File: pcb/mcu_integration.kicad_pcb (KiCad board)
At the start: 4 copper layers, 90.2 x 95.9 mm, 104 parts, among them IC1 TL7660IDGKR, IC10 AD844_OPAMP_MEL, IC2 TL081IDT, IC3 FOD814_OPTO_NOSHD, IC5 FOD814_OPTO_MEL, IC6 AD844_OPAMP_AL, IC7 FOD814_OPTO_AL, IC8 AD844_OPAMP_NOSHD, IC9 TL081IDT, J4 Conn_01x02, J5 DM3BT-DSF-PEJS, M1 MountingHole_Pad, M2 MountingHole_Pad, M3 MountingHole_Pad, M4 MountingHole_Pad, U1 STM32F103RBTx, U2 REF192_NOSHD, U3 REF192_AL, U4 REF192_MEL, U5 TPS2069CDBVR_MOSFET, U6 LM35DM

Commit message: Restructured PCB
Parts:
- removed C19, C20, C34, C38, C41: 0.1u, capstone:CAPC220145_88N_KEM-0.1u
- removed C21, C37: 1u, capstone:C0805-1u
- removed C23, C24: 10u, capstone:T495D
- removed C27: 100n, Capacitor_SMD:C_0402_1005Metric
- removed C33: 1u, Capacitor_SMD:C_0402_1005Metric
- removed C35, C36, C39, C40: 0.22u, capstone:C0805-0.22u
- removed C42: 150u, capstone:CAPC3225X280N_150U
- removed H1, H2: ESQ-126-39-L-D, capstone:ESQ-126-Y-X-D
- removed IC10: AD844_OPAMP_MEL, capstone:SOIC127P1032X265-16N-AD844
- removed IC3: FOD814_OPTO_NOSHD, capstone:SOP254P1016X385-4N-FOD
- removed IC5: FOD814_OPTO_MEL, capstone:SOP254P1016X385-4N-FOD
- removed IC8: AD844_OPAMP_NOSHD, capstone:SOIC127P1032X265-16N-AD844
- removed J4: Conn_01x02, Connector_PinHeader_2.54mm:PinHeader_1x02_P2.54mm_Vertical
- removed J5: DM3BT-DSF-PEJS, capstone:DM3BT_DSF_PEJS
- removed J_AD1, J_AD3: Conn_01x04, Connector_PinHeader_2.54mm:PinHeader_1x04_P2.54mm_Vertical
- removed M1, M2, M3, M4: MountingHole_Pad, MountingHole:MountingHole_3.2mm_M3_Pad_Via
- removed R15, R19: 820, Resistor_SMD:R_0402_1005Metric
- removed R16, R20: 47, Resistor_SMD:R_0402_1005Metric
- removed R17, R18, R29, R30: 100, Resistor_SMD:R_0402_1005Metric
- removed R28, R34: 100k, Resistor_SMD:R_0402_1005Metric
- removed R31, R35: 1k, Resistor_SMD:R_0402_1005Metric
- removed R33: 200, Resistor_SMD:R_0402_1005Metric
- removed U2: REF192_NOSHD, capstone:R_8_ADI-REF
- removed U4: REF192_MEL, capstone:R_8_ADI-REF
- removed U5: TPS2069CDBVR_MOSFET, capstone:DBV5_TEX_MF
- added PWR1: Conn_01x03, Connector_PinHeader_2.54mm:PinHeader_1x03_P2.54mm_Vertical, F.Cu at (142.6, 73.7)
- moved C22 44.4 mm to (193.3, 87.1)
- moved C29 44.4 mm to (201.1, 88.6)
- moved C32 44.4 mm to (193.3, 101.0)
- moved IC6 44.4 mm to (203.5, 96.2)
- moved IC7 44.4 mm to (185.4, 97.2)
- moved R25 44.4 mm to (209.6, 96.2)
- moved U3 44.4 mm to (193.3, 96.2)
- moved C28 44.4 mm to (193.3, 91.4)
- moved C30 44.4 mm to (206.3, 103.9)
- moved C31 44.4 mm to (193.2, 103.8)
- moved J_AD2 44.4 mm to (201.7, 113.2)
- moved R23 44.4 mm to (183.6, 103.8)
- moved R22 44.4 mm to (205.5, 89.6)
- moved R26 44.4 mm to (183.7, 90.1)
- moved R27 44.4 mm to (187.2, 90.1)
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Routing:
- net ADC1_IN0_SINE: track 215.7 -> 70.1 mm, vias 12 -> 5
- net -5V Output: track 172.1 -> 27.0 mm, vias 11 -> 3
- net 3.3V Output: track 109.1 -> 6.49 mm, vias 6 -> 0
- net GND: track 182.1 -> 85.8 mm, vias 41 -> 16
- net ADC1_IN1_OPAMP_NOSHD: track 90.3 -> 0.00 mm, vias 3 -> 0
- net ADC1_IN4_VREF_NOSHD: track 87.9 -> 0.00 mm
- net ADC1_IN12_OPTO_F_MEL: track 74.2 -> 0.00 mm, vias 2 -> 0
- net ADC1_IN5_VREF_MEL: track 68.0 -> 0.00 mm
- net ADC1_IN13_OPTO_E_MEL: track 63.2 -> 0.00 mm, vias 4 -> 0
- net +5V_EXT: track 56.5 -> 0.00 mm
- net ADC1_IN11_OPTO_E_NOSHD: track 52.8 -> 0.00 mm
- net ADC1_IN2_OPAMP_MEL: track 52.1 -> 0.00 mm, vias 4 -> 0
- net SIG_SQUARE: track 57.8 -> 6.64 mm, vias 3 -> 0
- net ADC1_IN3_OPAMP_AL: track 67.8 -> 25.6 mm, vias 2 -> 1
- net +5V: track 70.7 -> 29.3 mm, vias 17 -> 8
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- removed copper zone on In2.Cu, net +5V
- removed copper zone on In1.Cu, net GND
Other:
- board size 90.2 x 95.9 mm -> 50 x 50 mm

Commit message: Arranged components to fit board
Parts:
- C22, C28, C29, C30, C31, C32, IC6, IC7, R22, R23, R24, R25, R26, R27, U3: moved to B.Cu
- moved J_AD2 80.9 mm to (124.8, 88.1), turned to 0 degrees
- moved C30 75.1 mm to (134.1, 83.4), turned to 90 degrees
- moved R25 69.6 mm to (141.8, 80.2), turned to 0 degrees
- moved IC6 62.5 mm to (141.8, 86.3), turned to 180 degrees
- moved C31 59.4 mm to (134.2, 96.6), turned to 90 degrees
- moved R22 57.3 mm to (148.4, 84.3), turned to -90 degrees
- moved C32 56.5 mm to (137.0, 96.5), turned to 90 degrees
- moved C14 54.2 mm to (121.5, 105.8)
- moved C15 54.2 mm to (125.0, 105.8)
- moved C16 54.2 mm to (128.5, 105.8)
- moved C17 54.2 mm to (132.0, 105.8)
- moved C44 54.2 mm to (143.0, 105.8)
- moved J_SIG1 54.2 mm to (136.5, 107.5)
- moved C18 54.2 mm to (144.5, 116.4)
- moved C43 54.2 mm to (136.5, 112.0)
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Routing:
- net GND: track 85.8 -> 0.00 mm, vias 16 -> 0
- net ADC1_IN0_SINE: track 70.1 -> 0.00 mm, vias 5 -> 0
- net ADC1_IN15_OPTO_E_AL: track 35.3 -> 0.00 mm
- net ADC1_IN6_VREF_AL: track 32.8 -> 0.00 mm, vias 2 -> 0
- net +5V: track 29.3 -> 0.00 mm, vias 8 -> 0
- net -5V Output: track 27.0 -> 0.00 mm, vias 3 -> 0
- net ADC1_IN3_OPAMP_AL: track 25.6 -> 0.00 mm, vias 1 -> 0
- net ADC1_IN14_OPTO_F_AL: track 19.0 -> 0.00 mm, vias 2 -> 0
- net INVERT_SINE: track 18.7 -> 0.00 mm
- net RC_OUTPUT: track 13.8 -> 0.00 mm
- net Net-(IC9-INVERTING_INPUT): track 13.3 -> 0.00 mm
- net Net-(IC6--IN): track 9.63 -> 0.00 mm
- net Net-(IC2-INVERTING_INPUT): track 7.09 -> 0.00 mm
- net SIG_SQUARE: track 6.64 -> 0.00 mm
- net Net-(J_SIG1-Pin_1): track 6.61 -> 0.00 mm
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
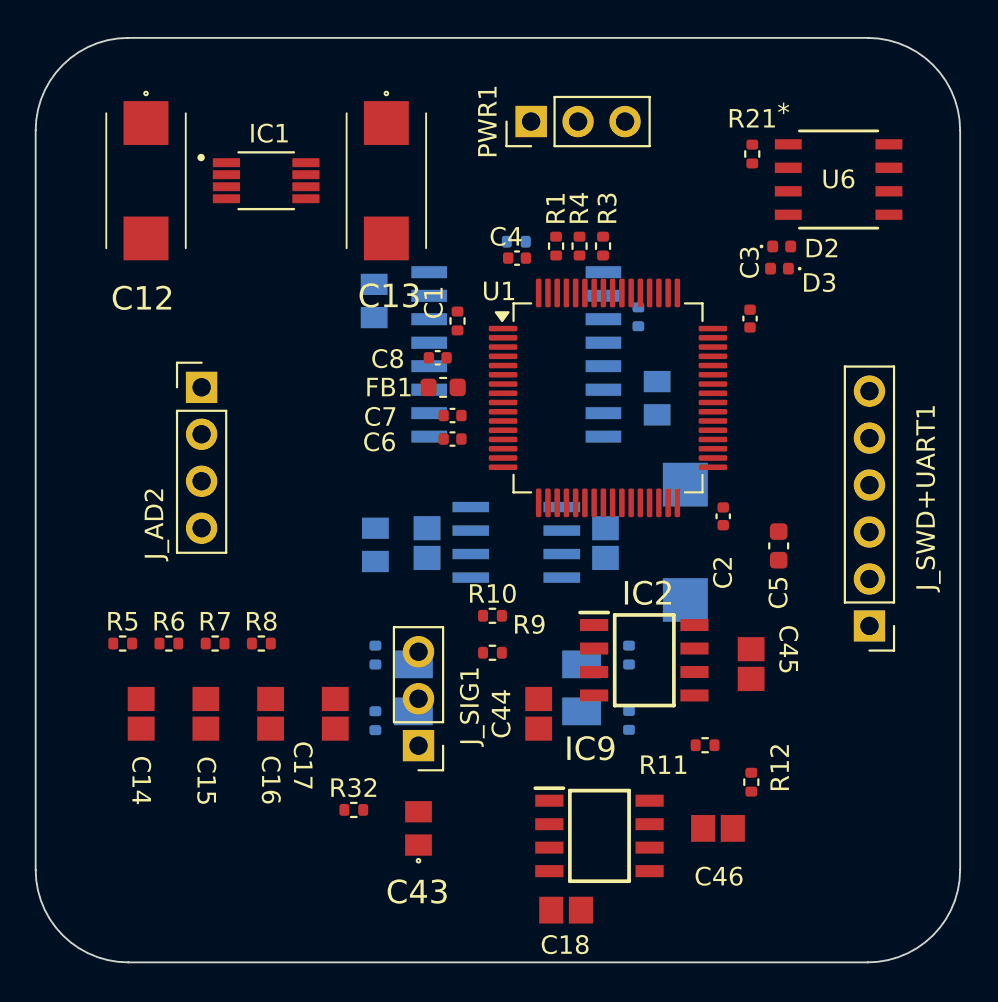
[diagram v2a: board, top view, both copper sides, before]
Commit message: Added two pin connector, routed all connections
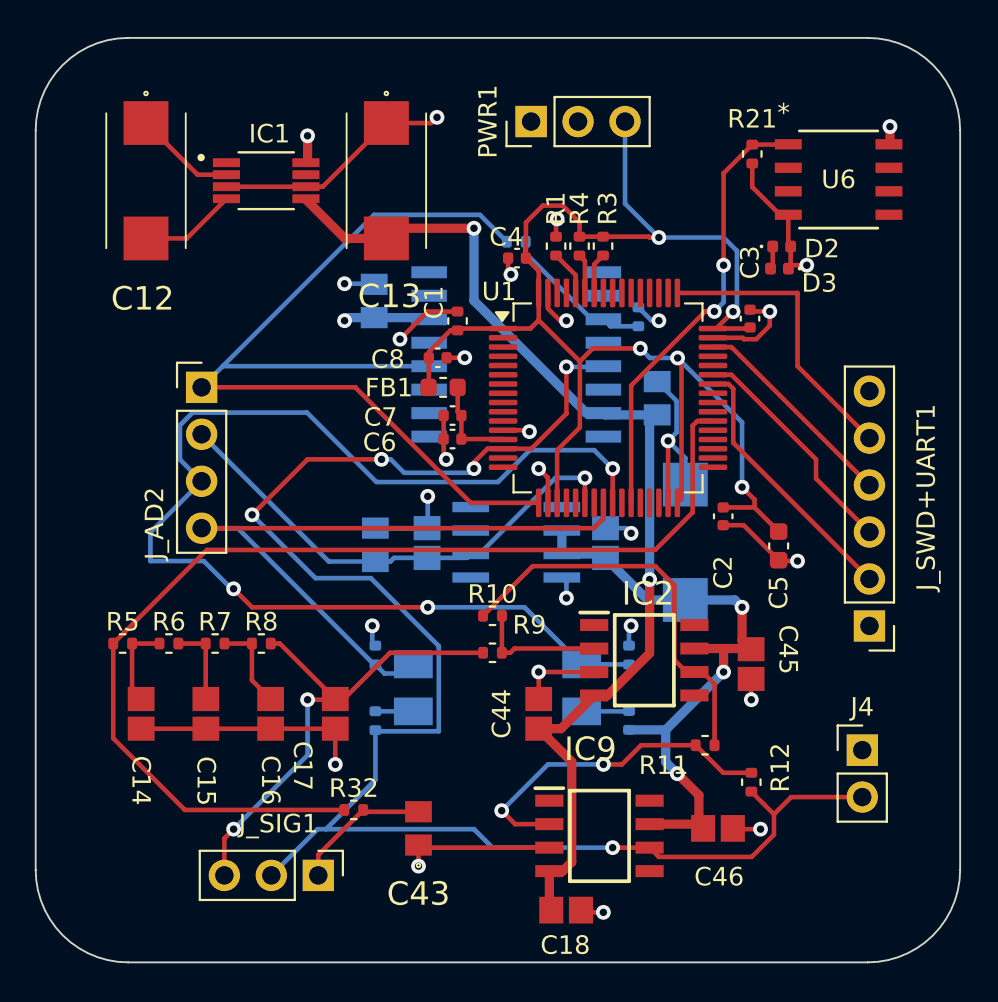
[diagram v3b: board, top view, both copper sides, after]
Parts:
- added J4: Conn_01x02, Connector_PinHeader_2.54mm:PinHeader_1x02_P2.54mm_Vertical, F.Cu at (160.5, 107.7)
- moved J_SIG1 8.86 mm to (131.1, 114.5), turned to -90 degrees
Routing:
- net GND: track 0.00 -> 97.2 mm, vias 0 -> 26
- net ADC1_IN0_SINE: track 0.00 -> 89.5 mm, vias 0 -> 5
- net 3.3V Output: track 0.00 -> 79.8 mm, vias 0 -> 5
- net ADC1_IN15_OPTO_E_AL: track 0.00 -> 65.4 mm, vias 0 -> 3
- net SIG_SQUARE: track 0.00 -> 59.4 mm
- net -5V Output: track 0.00 -> 59.0 mm, vias 0 -> 2
- net ADC1_IN3_OPAMP_AL: track 0.00 -> 53.0 mm
- net +5V: track 0.00 -> 41.7 mm, vias 0 -> 6
- net ADC1_IN14_OPTO_F_AL: track 0.00 -> 37.8 mm
- net ADC1_IN6_VREF_AL: track 0.00 -> 26.8 mm, vias 0 -> 1
- net RC_OUTPUT: track 0.00 -> 26.6 mm, vias 0 -> 2
- net ADC1_IN9_VREG_AL: track 0.00 -> 24.3 mm, vias 0 -> 2
- net INVERT_SINE: track 0.00 -> 22.0 mm
- net Net-(IC9-INVERTING_INPUT): track 0.00 -> 18.5 mm, vias 0 -> 2
- net /SWCLK: track 0.00 -> 16.0 mm
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- added copper zone on In2.Cu, net +5V
- added copper zone on In1.Cu, net GND

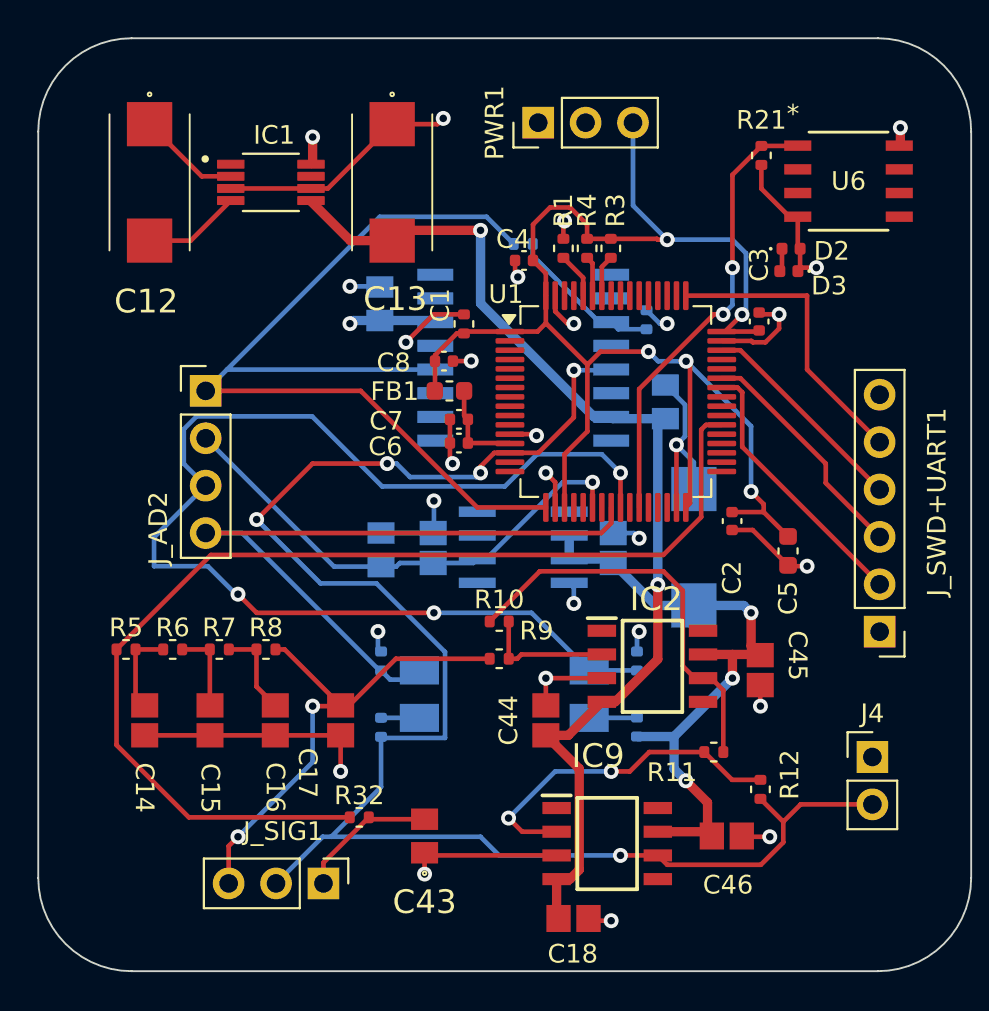
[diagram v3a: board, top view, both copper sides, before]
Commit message: Added I2C Connector
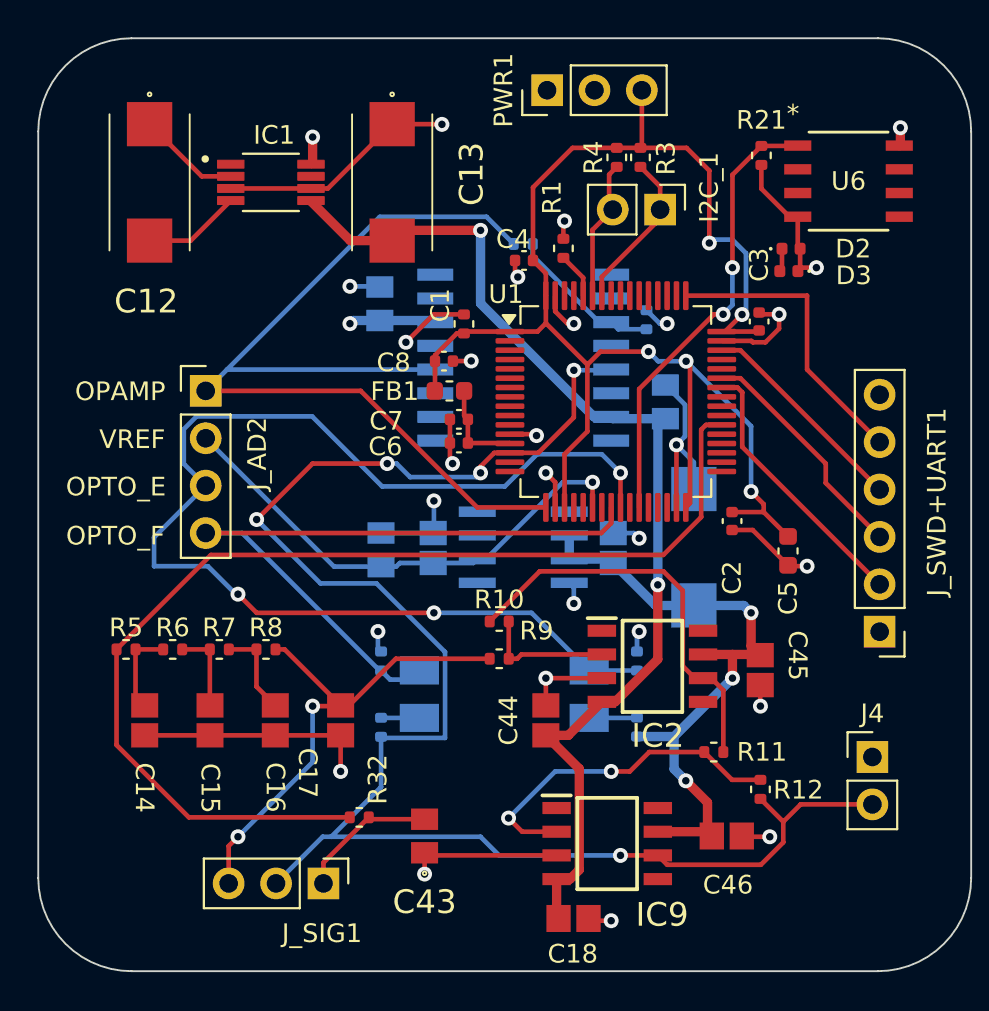
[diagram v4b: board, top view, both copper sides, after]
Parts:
- added I2C_1: Conn_01x02, Connector_PinHeader_2.54mm:PinHeader_1x02_P2.54mm_Vertical, F.Cu at (149.1, 78.4)
- moved R3 5.13 mm to (148.1, 75.6)
- moved R4 5.13 mm to (146.8, 75.6)
- moved PWR1 1.80 mm to (143.1, 72.0)
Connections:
- PWR1 pad 2: +5V_EXT -> +5V
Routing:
- net OBC_I2C_SCL: track 2.22 -> 8.63 mm
- net OBC_I2C_SDA: track 2.15 -> 7.60 mm
- net 3.3V Output: track 79.8 -> 81.6 mm
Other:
- board text added: "OPAMP"
- board text added: "OPTO_E"
- board text added: "OPTO_F"
- board text added: "VREF"

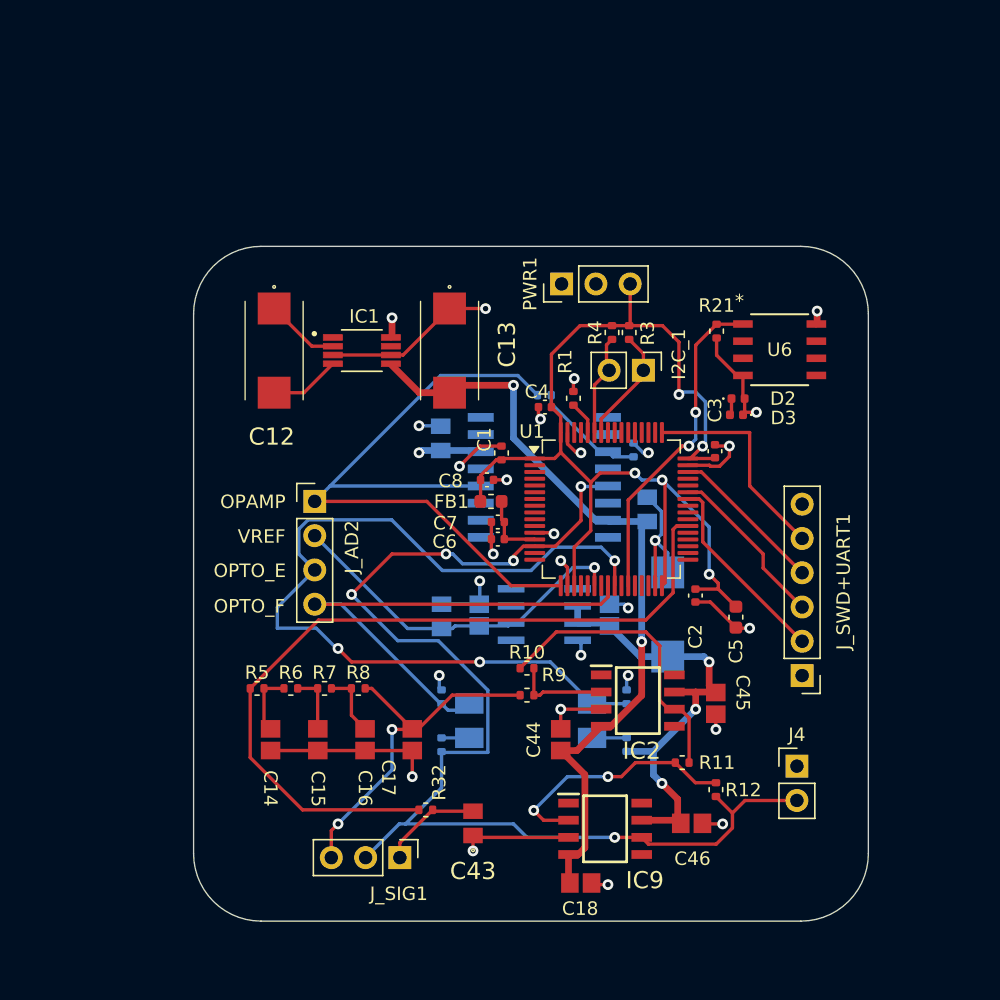
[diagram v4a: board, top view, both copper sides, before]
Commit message: Increased board size from 5x5 to 7x7
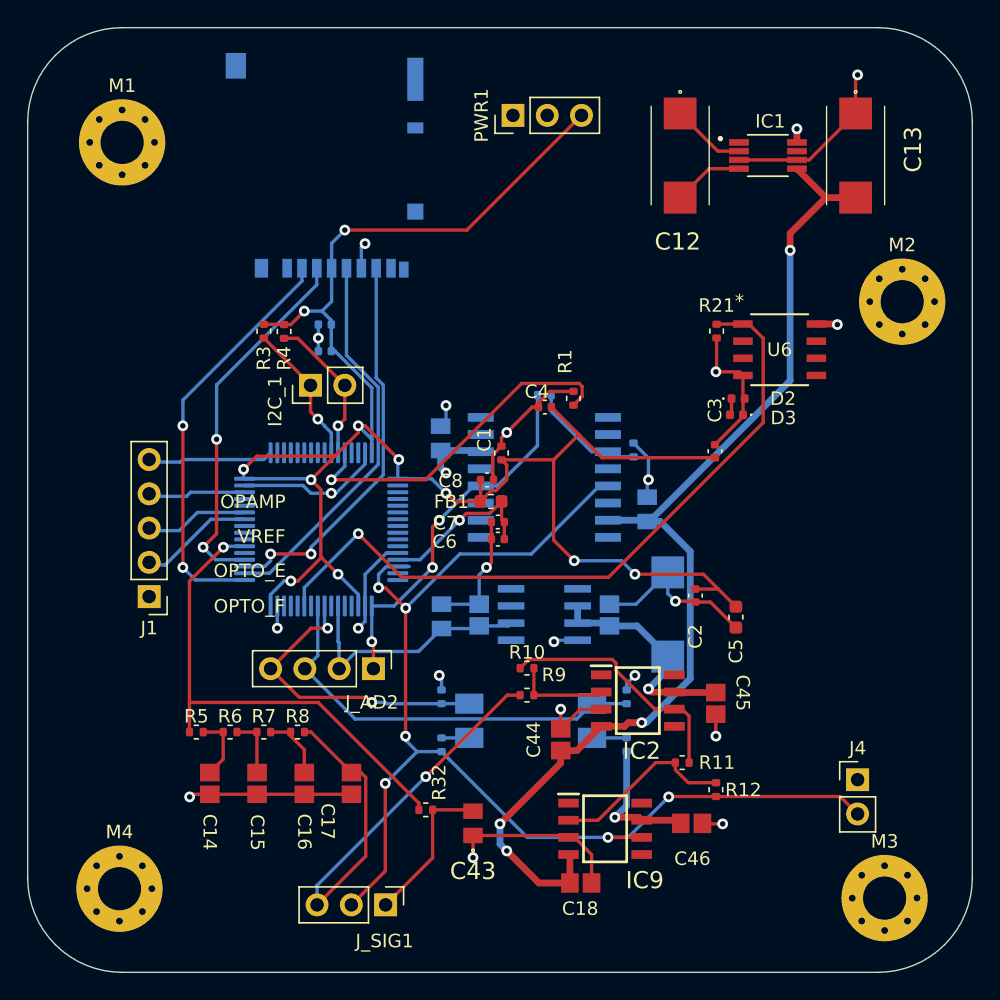
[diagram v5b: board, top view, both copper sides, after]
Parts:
- removed J_SWD+UART1: Conn_01x06, Connector_PinHeader_2.54mm:PinHeader_1x06_P2.54mm_Vertical
- added C27: 100n, Capacitor_SMD:C_0402_1005Metric, B.Cu at (125.5, 75.0)
- added C33: 1u, Capacitor_SMD:C_0402_1005Metric, B.Cu at (125.5, 77.0)
- added J1: Conn_01x05, Connector_PinHeader_2.54mm:PinHeader_1x05_P2.54mm_Vertical, F.Cu at (112.5, 95.2)
- added J5: DM3BT-DSF-PEJS, capstone:DM3BT_DSF_PEJS, B.Cu at (125.5, 63.0)
- added M1: MountingHole_Pad, MountingHole:MountingHole_3.2mm_M3_Pad_Via, F.Cu at (110.5, 61.5)
- added M2: MountingHole_Pad, MountingHole:MountingHole_3.2mm_M3_Pad_Via, F.Cu at (168.3, 73.3)
- added M3: MountingHole_Pad, MountingHole:MountingHole_3.2mm_M3_Pad_Via, F.Cu at (167.0, 117.5)
- added M4: MountingHole_Pad, MountingHole:MountingHole_3.2mm_M3_Pad_Via, F.Cu at (110.3, 116.8)
- U1: moved to B.Cu
- moved C13 33.4 mm to (164.8, 62.5)
- moved IC1 33.4 mm to (158.3, 62.5)
- moved C12 33.4 mm to (151.8, 62.5)
- moved R3 27.1 mm to (121.0, 75.5)
- moved I2C_1 24.7 mm to (124.5, 79.5), turned to 90 degrees
- moved R4 24.3 mm to (122.5, 75.5)
- moved U1 21.6 mm to (125.2, 90.2), turned to 180 degrees
- moved J_AD2 13.1 mm to (129.1, 100.5), turned to -90 degrees
- moved PWR1 13.0 mm to (139.5, 59.5)
- moved R5 5.54 mm to (116.0, 105.2)
- moved R6 5.54 mm to (118.5, 105.2)
- moved R7 5.54 mm to (121.0, 105.2)
- moved R8 5.54 mm to (123.5, 105.2)
- moved C14 5.54 mm to (117.0, 109.0)
- moved C15 5.54 mm to (120.5, 109.0)
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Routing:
- net 3.3V Output: track 81.6 -> 142.5 mm, vias 5 -> 11
- net ADC1_IN15_OPTO_E_AL: track 65.4 -> 30.9 mm, vias 3 -> 0
- net /SPI2_CS_NSS: track 0.00 -> 30.8 mm, vias 0 -> 2
- net /SPI2_MISO: track 0.00 -> 29.2 mm, vias 0 -> 2
- net ADC1_IN9_VREG_AL: track 24.3 -> 53.2 mm, vias 2 -> 1
- net /SPI2_SCK: track 0.00 -> 28.8 mm
- net /SPI2_MOSI: track 0.00 -> 27.6 mm, vias 0 -> 2
- net GND: track 97.0 -> 123.9 mm, vias 26 -> 20
- net ADC1_IN3_OPAMP_AL: track 53.0 -> 27.4 mm, vias 0 -> 3
- net /BOOT0: track 2.46 -> 25.7 mm, vias 0 -> 1
- net SIG_SQUARE: track 59.4 -> 36.9 mm, vias 0 -> 1
- net -5V Output: track 59.0 -> 80.4 mm, vias 2 -> 4
- net ADC1_IN14_OPTO_F_AL: track 37.8 -> 23.0 mm, vias 0 -> 2
- net RC_OUTPUT: track 26.6 -> 39.2 mm, vias 2 -> 1
- net ADC1_IN6_VREF_AL: track 26.8 -> 18.8 mm, vias 1 -> 0
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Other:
- board size 50 x 50 mm -> 70 x 70 mm
